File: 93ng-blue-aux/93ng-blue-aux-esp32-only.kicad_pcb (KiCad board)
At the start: 2 copper layers, 50 x 50 mm, 38 parts, among them J1 12V INPUT, J2 ESP32 UART, J3 USB_C_Receptacle_USB2.0, J7 I-BUS, Q1 S8050, Q2 S8050, SW1 PWR IN SELECT, U1 ESP32-WROOM-32D, U2 NCP1117-3.3_SOT223, U3 MC33897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

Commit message: Automatic freerouting job. Plot export
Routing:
- net GND: track 0.00 -> 258.0 mm
- net 3.3V: track 0.00 -> 140.2 mm
- net DTR: track 0.00 -> 73.6 mm
- net ESP32_EN: track 0.00 -> 50.5 mm, vias 0 -> 2
- net RTS: track 0.00 -> 43.0 mm, vias 0 -> 2
- net ESP32_RX: track 0.00 -> 42.6 mm, vias 0 -> 1
- net ESP32_TX: track 0.00 -> 41.6 mm, vias 0 -> 1
- net USB_D+: track 0.00 -> 31.8 mm, vias 0 -> 2
- net USB_D-: track 0.00 -> 24.6 mm, vias 0 -> 2
- net SW_CAN: track 0.00 -> 23.0 mm
- net USB_CC2: track 0.00 -> 21.5 mm
- net USB_VBUS: track 0.00 -> 20.5 mm, vias 0 -> 1
- net MC33_RX: track 0.00 -> 17.8 mm
- net MC33_TX: track 0.00 -> 16.7 mm, vias 0 -> 2
- net Net-(R3-Pad1): track 0.00 -> 16.6 mm, vias 0 -> 2
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
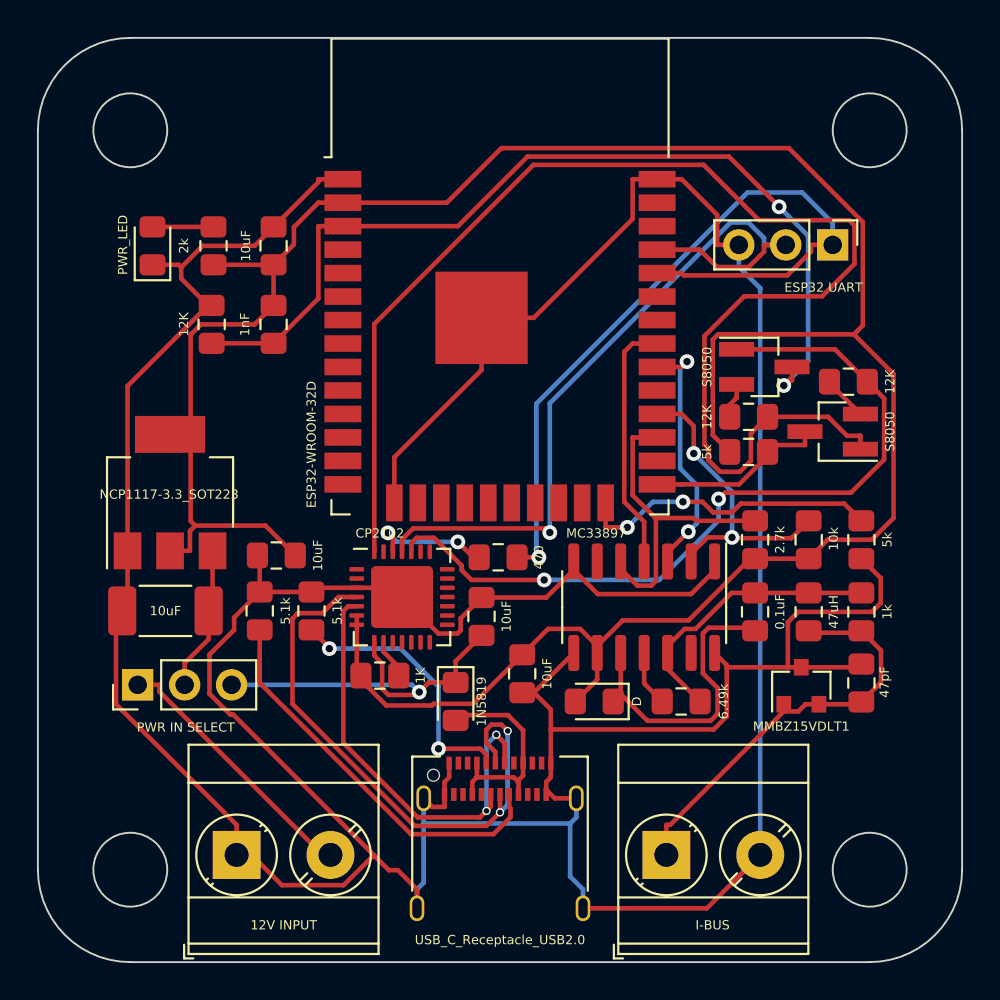
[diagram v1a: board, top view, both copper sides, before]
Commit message: Updated the input power select to be an actual switch, allowing easier access if in a stacked configuration.
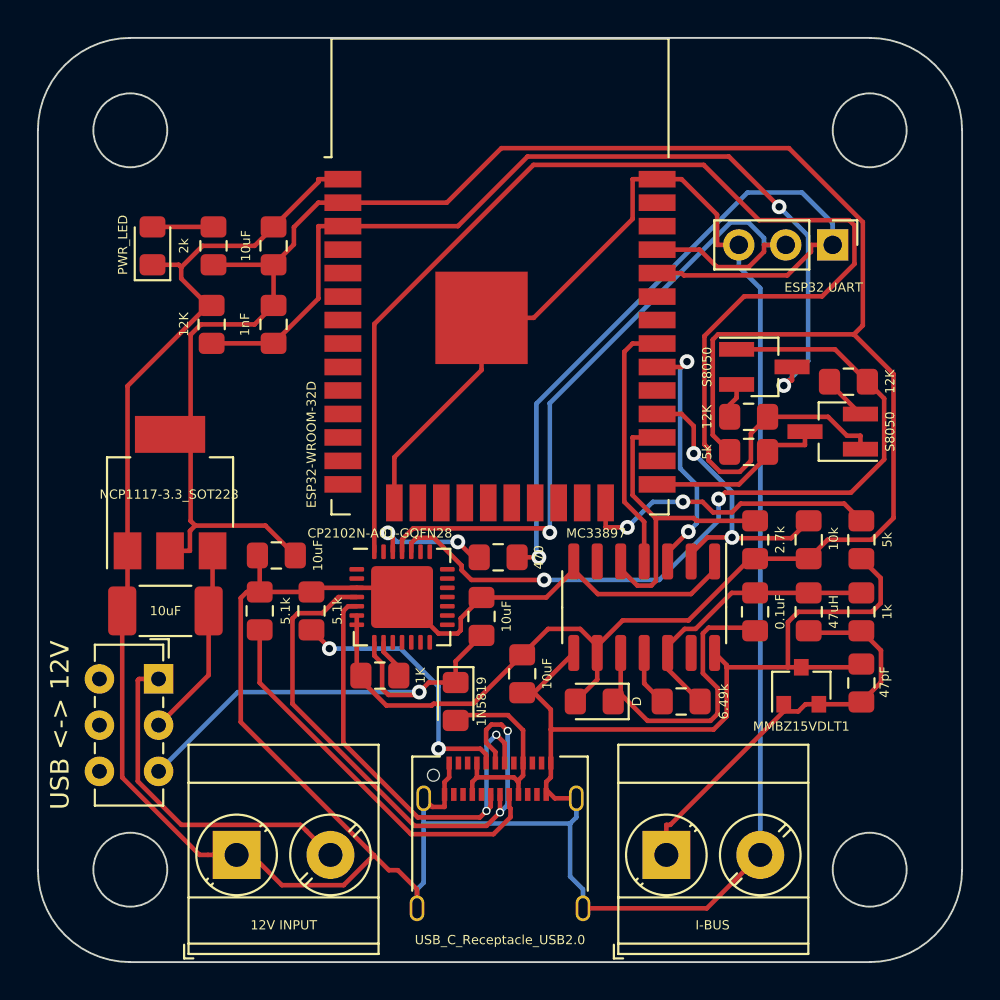
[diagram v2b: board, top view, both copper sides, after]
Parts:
- removed SW1: PWR IN SELECT, Connector_PinHeader_2.54mm:PinHeader_1x03_P2.54mm_Vertical
- added USB <-> 12V: PWR IN SELECT, Button_Switch_THT:SW_E-Switch_EG1271_DPDT, F.Cu at (176.5, 106.7)
- U5: value CP2102 -> CP2102N-A01-GQFN28
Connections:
- J3 pad A8: (no net) -> Net-(J3-PadA8)
- J3 pad B8: (no net) -> Net-(J3-PadB8)
- U1 pad 10: (no net) -> Net-(U1-Pad10)
- U1 pad 11: (no net) -> Net-(U1-Pad11)
- U1 pad 12: (no net) -> Net-(U1-Pad12)
- U1 pad 13: (no net) -> Net-(U1-Pad13)
- U1 pad 14: (no net) -> Net-(U1-Pad14)
- U1 pad 16: (no net) -> Net-(U1-Pad16)
- U1 pad 17: (no net) -> Net-(U1-Pad17)
- U1 pad 18: (no net) -> Net-(U1-Pad18)
- U1 pad 19: (no net) -> Net-(U1-Pad19)
- U1 pad 20: (no net) -> Net-(U1-Pad20)
- U1 pad 21: (no net) -> Net-(U1-Pad21)
- U1 pad 22: (no net) -> Net-(U1-Pad22)
- U1 pad 23: (no net) -> Net-(U1-Pad23)
- U1 pad 26: (no net) -> Net-(U1-Pad26)
- U1 pad 29: (no net) -> Net-(U1-Pad29)
- U1 pad 32: (no net) -> Net-(U1-Pad32)
- U1 pad 33: (no net) -> Net-(U1-Pad33)
- U1 pad 36: (no net) -> Net-(U1-Pad36)
- U1 pad 37: (no net) -> Net-(U1-Pad37)
- U1 pad 4: (no net) -> Net-(U1-Pad4)
- U1 pad 5: (no net) -> Net-(U1-Pad5)
- U1 pad 6: (no net) -> Net-(U1-Pad6)
- U1 pad 7: (no net) -> Net-(U1-Pad7)
- U1 pad 8: (no net) -> Net-(U1-Pad8)
- U1 pad 9: (no net) -> Net-(U1-Pad9)
- U3 pad 13: (no net) -> Net-(U3-Pad13)
- U3 pad 6: (no net) -> Net-(U3-Pad6)
- U5 pad 1: (no net) -> Net-(U5-Pad1)
- U5 pad 10: (no net) -> Net-(U5-Pad10)
- U5 pad 11: (no net) -> Net-(U5-Pad11)
- U5 pad 12: (no net) -> Net-(U5-Pad12)
- U5 pad 13: (no net) -> Net-(U5-Pad13)
- U5 pad 14: (no net) -> Net-(U5-Pad14)
- U5 pad 15: (no net) -> Net-(U5-Pad15)
- U5 pad 16: (no net) -> Net-(U5-Pad16)
- U5 pad 17: (no net) -> Net-(U5-Pad17)
- U5 pad 18: (no net) -> Net-(U5-Pad18)
- U5 pad 19: (no net) -> Net-(U5-Pad19)
- U5 pad 2: (no net) -> Net-(U5-Pad2)
- U5 pad 20: (no net) -> Net-(U5-Pad20)
- U5 pad 21: (no net) -> Net-(U5-Pad21)
- U5 pad 22: (no net) -> Net-(U5-Pad22)
- U5 pad 23: (no net) -> Net-(U5-Pad23)
- U5 pad 27: (no net) -> Net-(U5-Pad27)
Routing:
- net USB_VBUS: track 20.5 -> 26.1 mm
- net Net-(J1-Pad2): track 14.5 -> 19.1 mm
- net Net-(C1-Pad1): track 7.88 -> 10.6 mm
- net GND: track 258.0 -> 259.1 mm

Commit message: Working on saab board interconnect
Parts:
- added J4: Conn_02x16_Row_Letter_First, Connector_PinHeader_1.00mm:PinHeader_2x16_P1.00mm_Vertical, F.Cu at (171.2, 82.3)
- SW1: renamed from USB <-> 12V
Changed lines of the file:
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@@
     (tracks 456)
     (zones 0)
-    (modules 38)
+    (modules 39)
     (nets 77)
   )
@@
     (descr "E-Switch sub miniature slide switch, EG series, DPDT, http://spec_sheets.e-switch.com/specs/P040047.pdf")
     (tags "switch DPDT")
-    (fp_text reference "USB <-> 12V" (at 2.5 5.334 90) (layer F.SilkS)
+    (fp_text reference SW1 (at 2.5 5.334 90) (layer F.SilkS)
       (effects (font (size 1 1) (thickness 0.2)))
     )
@@
     )
   )
+  (module Connector_PinHeader_1.00mm:PinHeader_2x16_P1.00mm_Vertical (layer F.Cu)
+    (at 171.196 82.296)
+    (descr "Through hole straight pin header, 2x16, 1.00mm pitch, double rows")
+    (tags "Through hole pin header THT 2x16 1.00mm double row")
+    (fp_text reference J4 (at 0.5 -1.56) (layer F.SilkS)
+      (effects (font (size 1 1) (thickness 0.15)))
+    )
+    (fp_text value Conn_02x16_Row_Letter_First (at 0.5 16.56) (layer F.Fab)
+      (effects (font (size 1 1) (thickness 0.15)))
+    )
+    (fp_line (start -0.075 -0.5) (end 1.65 -0.5) (layer F.Fab) (width 0.1))
+    (fp_line (start 1.65 -0.5) (end 1.65 15.5) (layer F.Fab) (width 0.1))
+    (fp_line (start 1.65 15.5) (end -0.65 15.5) (layer F.Fab) (width 0.1))
+    (fp_line (start -0.65 15.5) (end -0.65 0.075) (layer F.Fab) (width 0.1))
+    (fp_line (start -0.65 0.075) (end -0.075 -0.5) (layer F.Fab) (width 0.1))
+    (fp_line (start -0.71 15.56) (end -0.394493 15.56) (layer F.SilkS) (width 0.12))
+    (fp_line (start 1.394493 15.56) (end 1.71 15.56) (layer F.SilkS) (width 0.12))
+    (fp_line (start 0.394493 15.56) (end 0.605507 15.56) (layer F.SilkS) (width 0.12))
+    (fp_line (start -0.71 0.685) (end -0.71 15.56) (layer F.SilkS) (width 0.12))
+    (fp_line (start 1.71 -0.56) (end 1.71 15.56) (layer F.SilkS) (width 0.12))
+    (fp_line (start -0.71 0.685) (end -0.608276 0.685) (layer F.SilkS) (width 0.12))
+    (fp_line (start 1.394493 -0.56) (end 1.71 -0.56) (layer F.SilkS) (width 0.12))
+    (fp_line (start -0.71 0) (end -0.71 -0.685) (layer F.SilkS) (width 0.12))
+    (fp_line (start -0.71 -0.685) (end 0 -0.685) (layer F.SilkS) (width 0.12))
+    (fp_line (start -1.15 -1) (end -1.15 16) (layer F.CrtYd) (width 0.05))
+    (fp_line (start -1.15 16) (end 2.15 16) (layer F.CrtYd) (width 0.05))
+    (fp_line (start 2.15 16) (end 2.15 -1) (layer F.CrtYd) (width 0.05))
+    (fp_line (start 2.15 -1) (end -1.15 -1) (layer F.CrtYd) (width 0.05))
+    (fp_text user %R (at 0.5 7.5 90) (layer F.Fab)
+      (effects (font (size 1 1) (thickness 0.15)))
+    )
+    (pad 1 thru_hole rect (at 0 0) (size 0.85 0.85) (drill 0.5) (layers *.Cu *.Mask))
+    (pad 2 thru_hole oval (at 1 0) (size 0.85 0.85) (drill 0.5) (layers *.Cu *.Mask))
+    (pad 3 thru_hole oval (at 0 1) (size 0.85 0.85) (drill 0.5) (layers *.Cu *.Mask))
+    (pad 4 thru_hole oval (at 1 1) (size 0.85 0.85) (drill 0.5) (layers *.Cu *.Mask))
+    (pad 5 thru_hole oval (at 0 2) (size 0.85 0.85) (drill 0.5) (layers *.Cu *.Mask))
+    (pad 6 thru_hole oval (at 1 2) (size 0.85 0.85) (drill 0.5) (layers *.Cu *.Mask))
+    (pad 7 thru_hole oval (at 0 3) (size 0.85 0.85) (drill 0.5) (layers *.Cu *.Mask))
+    (pad 8 thru_hole oval (at 1 3) (size 0.85 0.85) (drill 0.5) (layers *.Cu *.Mask))
+    (pad 9 thru_hole oval (at 0 4) (size 0.85 0.85) (drill 0.5) (layers *.Cu *.Mask))
+    (pad 10 thru_hole oval (at 1 4) (size 0.85 0.85) (drill 0.5) (layers *.Cu *.Mask))
+    (pad 11 thru_hole oval (at 0 5) (size 0.85 0.85) (drill 0.5) (layers *.Cu *.Mask))
+    (pad 12 thru_hole oval (at 1 5) (size 0.85 0.85) (drill 0.5) (layers *.Cu *.Mask))
+    (pad 13 thru_hole oval (at 0 6) (size 0.85 0.85) (drill 0.5) (layers *.Cu *.Mask))
+    (pad 14 thru_hole oval (at 1 6) (size 0.85 0.85) (drill 0.5) (layers *.Cu *.Mask))
+    (pad 15 thru_hole oval (at 0 7) (size 0.85 0.85) (drill 0.5) (layers *.Cu *.Mask))
+    (pad 16 thru_hole oval (at 1 7) (size 0.85 0.85) (drill 0.5) (layers *.Cu *.Mask))
+    (pad 17 thru_hole oval (at 0 8) (size 0.85 0.85) (drill 0.5) (layers *.Cu *.Mask))
+    (pad 18 thru_hole oval (at 1 8) (size 0.85 0.85) (drill 0.5) (layers *.Cu *.Mask))
+    (pad 19 thru_hole oval (at 0 9) (size 0.85 0.85) (drill 0.5) (layers *.Cu *.Mask))
+    (pad 20 thru_hole oval (at 1 9) (size 0.85 0.85) (drill 0.5) (layers *.Cu *.Mask))
+    (pad 21 thru_hole oval (at 0 10) (size 0.85 0.85) (drill 0.5) (layers *.Cu *.Mask))
+    (pad 22 thru_hole oval (at 1 10) (size 0.85 0.85) (drill 0.5) (layers *.Cu *.Mask))
+    (pad 23 thru_hole oval (at 0 11) (size 0.85 0.85) (drill 0.5) (layers *.Cu *.Mask))
+    (pad 24 thru_hole oval (at 1 11) (size 0.85 0.85) (drill 0.5) (layers *.Cu *.Mask))
+    (pad 25 thru_hole oval (at 0 12) (size 0.85 0.85) (drill 0.5) (layers *.Cu *.Mask))
+    (pad 26 thru_hole oval (at 1 12) (size 0.85 0.85) (drill 0.5) (layers *.Cu *.Mask))
+    (pad 27 thru_hole oval (at 0 13) (size 0.85 0.85) (drill 0.5) (layers *.Cu *.Mask))
+    (pad 28 thru_hole oval (at 1 13) (size 0.85 0.85) (drill 0.5) (layers *.Cu *.Mask))
+    (pad 29 thru_hole oval (at 0 14) (size 0.85 0.85) (drill 0.5) (layers *.Cu *.Mask))
+    (pad 30 thru_hole oval (at 1 14) (size 0.85 0.85) (drill 0.5) (layers *.Cu *.Mask))
+    (pad 31 thru_hole oval (at 0 15) (size 0.85 0.85) (drill 0.5) (layers *.Cu *.Mask))
+    (pad 32 thru_hole oval (at 1 15) (size 0.85 0.85) (drill 0.5) (layers *.Cu *.Mask))
+    (model ${KISYS3DMOD}/Connector_PinHeader_1.00mm.3dshapes/PinHeader_2x16_P1.00mm_Vertical.wrl
+      (at (xyz 0 0 0))
+      (scale (xyz 1 1 1))
+      (rotate (xyz 0 0 0))
+    )
+  )
   (gr_line (start 217 97) (end 195 119) (layer Margin) (width 0.15))
   (gr_line (start 195 75) (end 195 119) (layer Margin) (width 0.15))
@@
   (segment (start 179.45 99.75) (end 179.45 102.7875) (width 0.25) (layer F.Cu) (net 1) (status 30))
   (segment (start 179.45 102.7875) (end 179.2375 103) (width 0.25) (layer F.Cu) (net 1) (status 30))
-  (segment (start 179.2375 106.4725) (end 179.2375 103) (width 0.25) (layer F.Cu) (net 1))
-  (segment (start 176.53 109.18) (end 179.2375 106.4725) (width 0.25) (layer F.Cu) (net 1))
+  (segment (start 179.2375 106.4725) (end 179.2375 103) (width 0.25) (layer F.Cu) (net 1) (status 20))
+  (segment (start 176.53 109.18) (end 179.2375 106.4725) (width 0.25) (layer F.Cu) (net 1) (status 10))
   (segment (start 186.5 79.645) (end 185.1747 79.645) (width 0.25) (layer F.Cu) (net 2) (status 10))
   (segment (start 209.08 116.2) (end 206.19 119.09) (width 0.25) (layer F.Cu) (net 2) (status 10))
@@
   (segment (start 174.85 102.7125) (end 174.5625 103) (width 0.25) (layer F.Cu) (net 2) (status 30))
   (segment (start 174.5625 103) (end 174.2246 103.3379) (width 0.25) (layer F.Cu) (net 2) (status 30))
-  (segment (start 181.3 101.975) (end 182 101.975) (width 0.25) (layer F.Cu) (net 2))
-  (segment (start 180.97499 102.30001) (end 181.3 101.975) (width 0.25) (layer F.Cu) (net 2))
+  (segment (start 181.3 101.975) (end 182 101.975) (width 0.25) (layer F.Cu) (net 2) (status 30))
+  (segment (start 180.97499 102.30001) (end 181.3 101.975) (width 0.25) (layer F.Cu) (net 2) (status 20))
   (segment (start 180.97499 109.01529) (end 180.97499 102.30001) (width 0.25) (layer F.Cu) (net 2))
   (segment (start 188.1704 116.2107) (end 180.97499 109.01529) (width 0.25) (layer F.Cu) (net 2))
   (segment (start 178.748588 116.2) (end 179.2 116.2) (width 0.25) (layer F.Cu) (net 2))
-  (segment (start 179.2 116.2) (end 180.75 116.2) (width 0.25) (layer F.Cu) (net 2))
+  (segment (start 179.2 116.2) (end 180.75 116.2) (width 0.25) (layer F.Cu) (net 2) (status 20))
   (segment (start 174.5625 112.013912) (end 178.748588 116.2) (width 0.25) (layer F.Cu) (net 2))
-  (segment (start 174.5625 103) (end 174.5625 112.013912) (width 0.25) (layer F.Cu) (net 2))
+  (segment (start 174.5625 103) (end 174.5625 112.013912) (width 0.25) (layer F.Cu) (net 2) (status 10))
   (segment (start 182.75 84.275) (end 179.5 84.275) (width 0.25) (layer F.Cu) (net 3) (status 30))
   (segment (start 177.15 93.45) (end 178.2627 93.45) (width 0.25) (layer F.Cu) (net 3) (status 30))
@@
   (via (at 190.6319 107.3906) (size 0.8) (layers F.Cu B.Cu) (net 14))
   (segment (start 180.8194 107.3906) (end 190.6319 107.3906) (width 0.25) (layer B.Cu) (net 14))
-  (segment (start 176.53 111.68) (end 180.8194 107.3906) (width 0.25) (layer B.Cu) (net 14))
+  (segment (start 176.53 111.68) (end 180.8194 107.3906) (width 0.25) (layer B.Cu) (net 14) (status 10))
   (segment (start 192.6 108.925) (end 192.887 108.638) (width 0.25) (layer F.Cu) (net 15) (status 30))
   (segment (start 192.887 108.638) (end 195.4307 108.638) (width 0.25) (layer F.Cu) (net 15) (status 10))
@@
   (segment (start 177.759997 114.574999) (end 184.204999 114.574999) (width 0.25) (layer F.Cu) (net 16))
   (segment (start 175.404999 106.755001) (end 175.404999 112.220001) (width 0.25) (layer F.Cu) (net 16))
-  (segment (start 184.530001 114.900001) (end 185.83 116.2) (width 0.25) (layer F.Cu) (net 16))
+  (segment (start 184.530001 114.900001) (end 185.83 116.2) (width 0.25) (layer F.Cu) (net 16) (status 20))
   (segment (start 175.48 106.68) (end 175.404999 106.755001) (width 0.25) (layer F.Cu) (net 16))
-  (segment (start 176.53 106.68) (end 175.48 106.68) (width 0.25) (layer F.Cu) (net 16))
+  (segment (start 176.53 106.68) (end 175.48 106.68) (width 0.25) (layer F.Cu) (net 16) (status 10))
   (segment (start 211.8247 83.2) (end 211.8247 83.5673) (width 0.25) (layer F.Cu) (net 17))
   (segment (start 211.8247 83.5673) (end 210.5434 84.8486) (width 0.25) (layer F.Cu) (net 17))
